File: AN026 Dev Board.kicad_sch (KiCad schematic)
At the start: 1 part

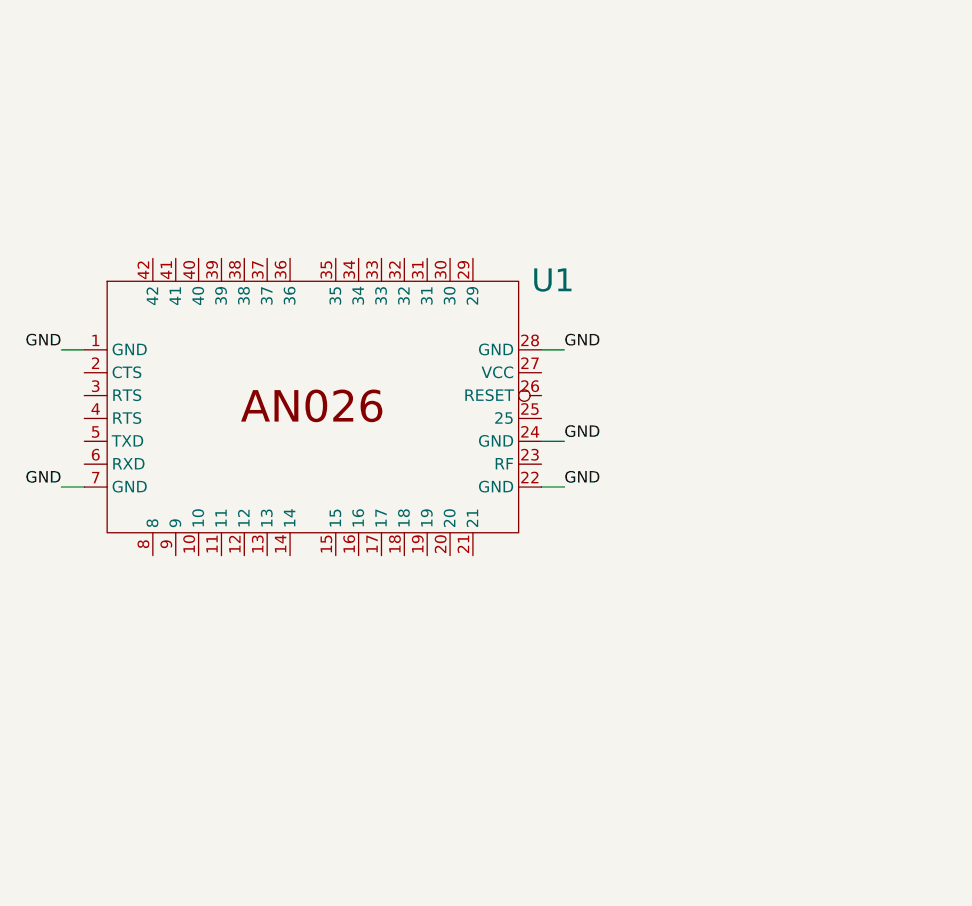
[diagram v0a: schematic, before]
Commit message: Updated symbols, Made schematic and routed traces.
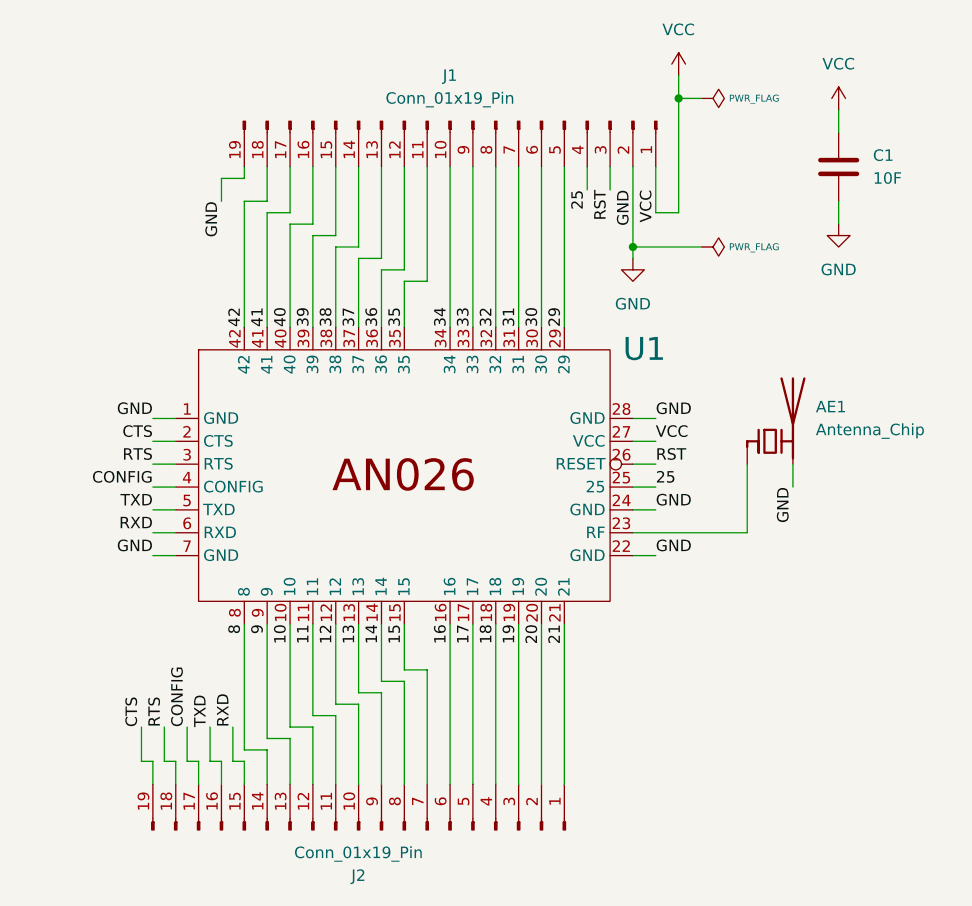
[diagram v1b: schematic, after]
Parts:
- added AE1: Antenna_Chip, RF_Antenna:Texas_SWRA117D_2.4GHz_Left, symbol Device:Antenna_Chip
- added C1: 10F, Capacitor_SMD:C_0805_2012Metric_Pad1.18x1.45mm_HandSolder, symbol Device:C
- added J1, J2: Conn_01x19_Pin, Connector_PinSocket_2.54mm:PinSocket_1x19_P2.54mm_Vertical, symbol Connector:Conn_01x19_Pin
- U1: footprint RC2400:RC2400 -> AN026:AN026
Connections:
- net GND: now also AE1.2 (PCB_Trace), C1.2, J1.19 (Pin_19), J1.2 (Pin_2)
- net 10: now reaches U1.10
- net 10: now also J2.12 (Pin_12)
- net 11: now reaches U1.11
- net 11: now also J2.11 (Pin_11)
- net 12: now reaches U1.12
- net 12: now also J2.10 (Pin_10)
- net 13: now reaches U1.13
- net 13: now also J2.9 (Pin_9)
- net 14: now reaches U1.14
- net 14: now also J2.8 (Pin_8)
- net 15: now reaches U1.15
- net 15: now also J2.7 (Pin_7)
- net 16: now reaches U1.16
- net 16: now also J2.6 (Pin_6)
- net 17: now reaches U1.17
- net 17: now also J2.5 (Pin_5)
- net 18: now reaches U1.18
- net 18: now also J2.4 (Pin_4)
- net 19: now reaches U1.19
- net 19: now also J2.3 (Pin_3)
- net CTS: now reaches U1.2 (CTS)
- net CTS: now also J2.19 (Pin_19)
- net 20: now reaches U1.20
- net 20: now also J2.2 (Pin_2)
- net 21: now reaches U1.21
- net 21: now also J2.1 (Pin_1)
- net at U1.23 (RF): now also AE1.1 (FEED)
- net 25: now reaches U1.25
- net 25: now also J1.4 (Pin_4)
- net RST: now reaches U1.26 (RESET)
- net RST: now also J1.3 (Pin_3)
- net VCC: now reaches U1.27 (VCC)
- net VCC: now also C1.1, J1.1 (Pin_1)
- net 29: now reaches U1.29
- net 29: now also J1.5 (Pin_5)
- net RTS: now reaches U1.3 (RTS)
- net RTS: now also J2.18 (Pin_18)
- net 30: now reaches U1.30
- net 30: now also J1.6 (Pin_6)
- net 31: now reaches U1.31
- net 31: now also J1.7 (Pin_7)
- net 32: now reaches U1.32
- net 32: now also J1.8 (Pin_8)
- net 33: now reaches U1.33
- net 33: now also J1.9 (Pin_9)
- net 34: now reaches U1.34
- net 34: now also J1.10 (Pin_10)
- net 35: now reaches U1.35
- net 35: now also J1.11 (Pin_11)
- net 36: now reaches U1.36
- net 36: now also J1.12 (Pin_12)
- net 37: now reaches U1.37
- net 37: now also J1.13 (Pin_13)
- net 38: now reaches U1.38
- net 38: now also J1.14 (Pin_14)
- net 39: now reaches U1.39
- net 39: now also J1.15 (Pin_15)
- net CONFIG: now reaches U1.4 (CONFIG)
- net CONFIG: now also J2.17 (Pin_17)
- net 40: now reaches U1.40
- net 40: now also J1.16 (Pin_16)
- net 41: now reaches U1.41
- net 41: now also J1.17 (Pin_17)
- net 42: now reaches U1.42
- net 42: now also J1.18 (Pin_18)
- net TXD: now reaches U1.5 (TXD)
- net TXD: now also J2.16 (Pin_16)
- net RXD: now reaches U1.6 (RXD)
- net RXD: now also J2.15 (Pin_15)
- net 8: now reaches U1.8
- net 8: now also J2.14 (Pin_14)
- net 9: now reaches U1.9
- net 9: now also J2.13 (Pin_13)
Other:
- moved on the sheet: U1

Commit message: Finished up the PCB.
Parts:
- J1, J2: footprint Connector_PinSocket_2.54mm:PinSocket_1x19_P2.54mm_Vertical -> Connector_PinHeader_2.54mm:PinHeader_1x19_P2.54mm_Vertical
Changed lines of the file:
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@@
 			)
 		)
-		(property "Footprint" "Connector_PinSocket_2.54mm:PinSocket_1x19_P2.54mm_Vertical"
+		(property "Footprint" "Connector_PinHeader_2.54mm:PinHeader_1x19_P2.54mm_Vertical"
 			(at 143.51 137.16 0)
 			(effects
@@
 			)
 		)
-		(property "Footprint" "Connector_PinSocket_2.54mm:PinSocket_1x19_P2.54mm_Vertical"
+		(property "Footprint" "Connector_PinHeader_2.54mm:PinHeader_1x19_P2.54mm_Vertical"
 			(at 153.67 58.42 0)
 			(effects
